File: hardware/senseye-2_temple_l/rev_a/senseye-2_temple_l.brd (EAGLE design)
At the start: 142.5 x 43.2 mm, 1 part

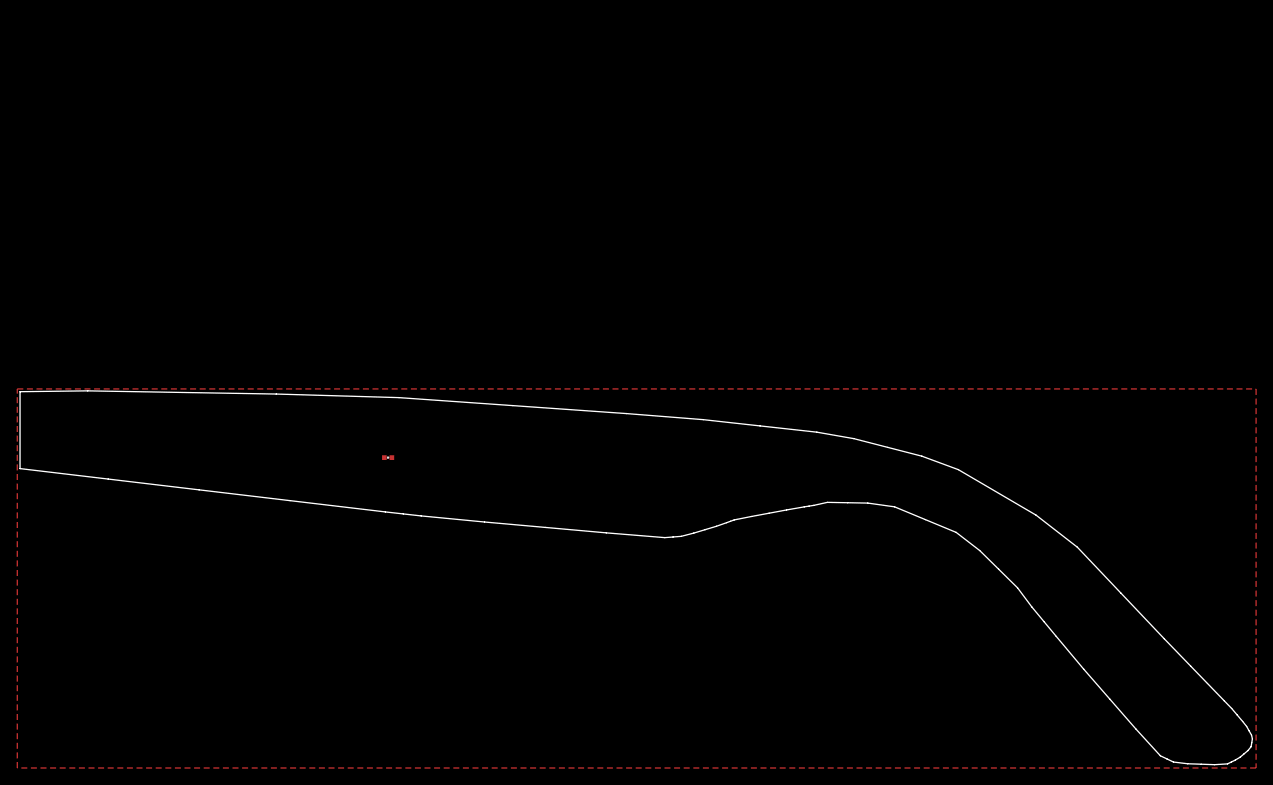
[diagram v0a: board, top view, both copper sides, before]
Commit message: moved all to 0,0 origin
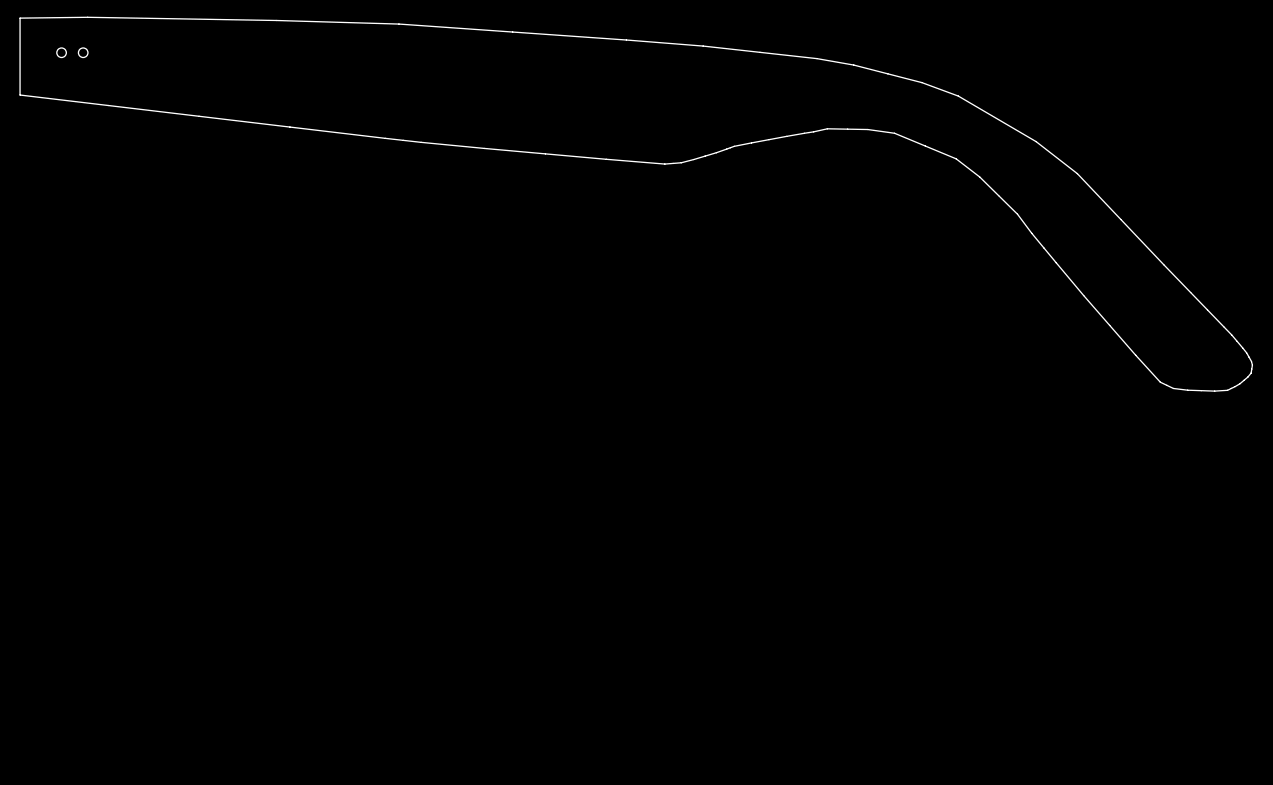
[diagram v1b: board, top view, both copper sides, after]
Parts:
- removed R1: (no value), passives:0402_RES
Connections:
- removed net GND: R1.1, R1.2
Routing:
- removed copper zone on layer 1, net GND
